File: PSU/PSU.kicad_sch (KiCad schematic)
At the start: 27 parts, among them J1 Screw_Terminal_01x02, U1 STPS10L25G-TR, U2 STPS10L25G-TR, U3 L4975A

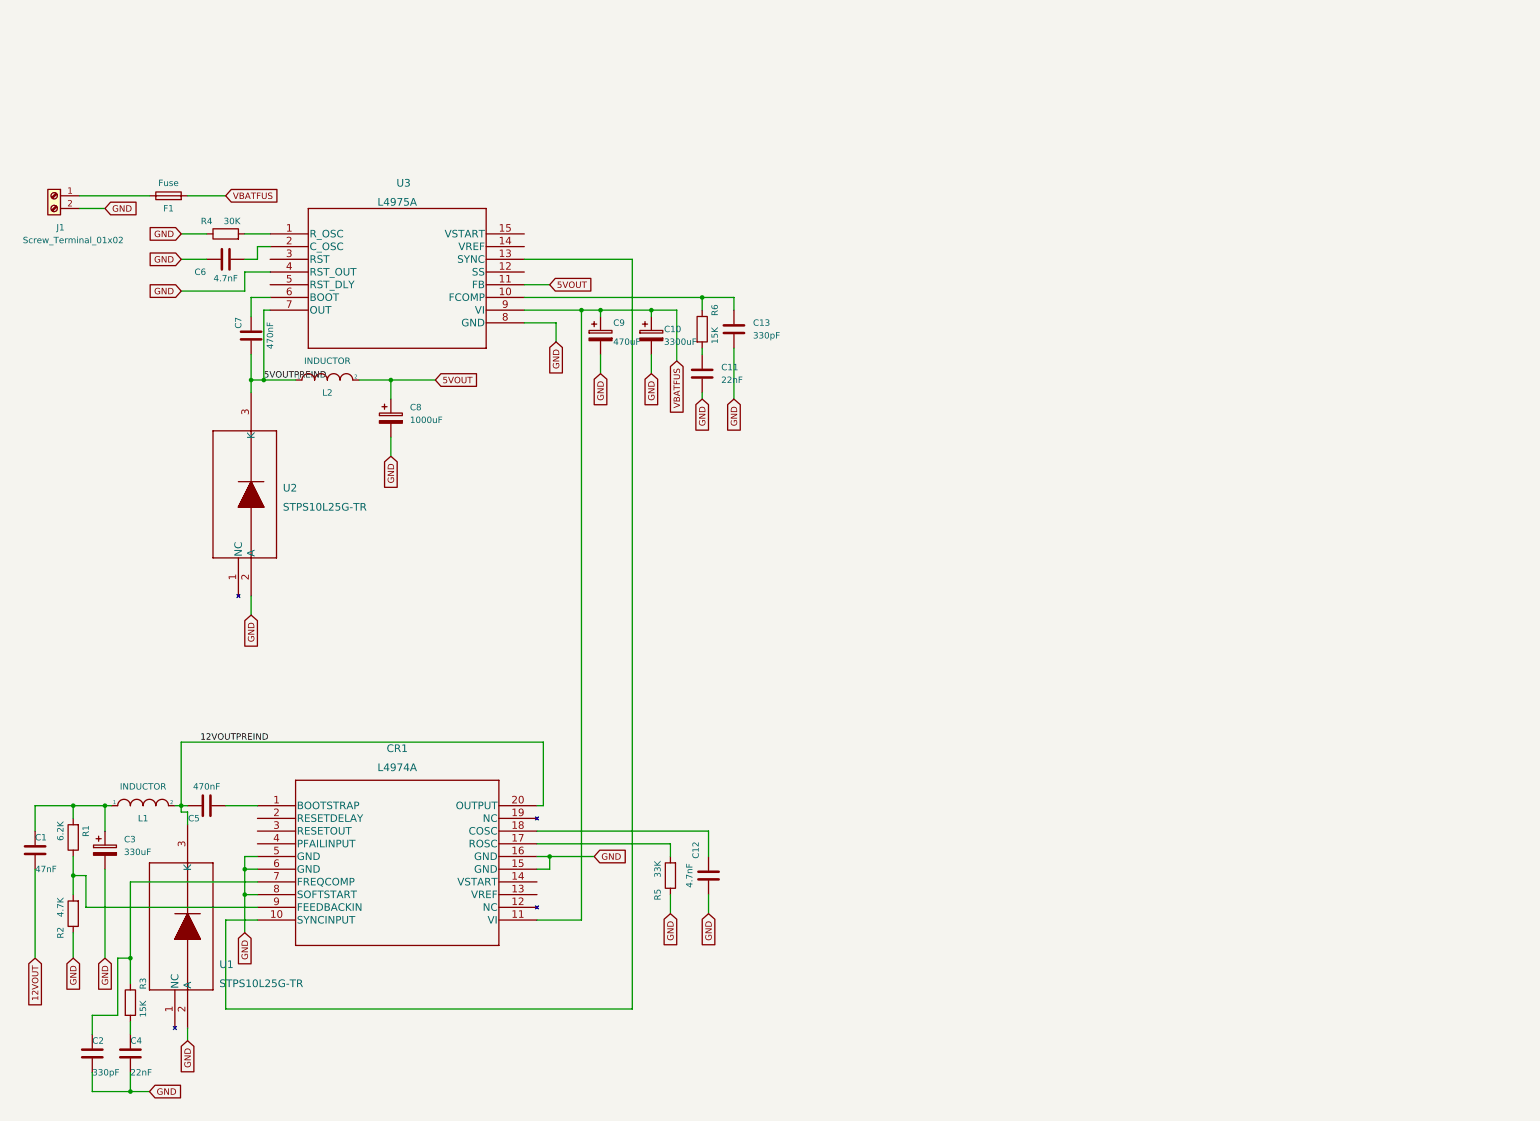
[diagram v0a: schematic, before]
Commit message: PCB placed and routed, more work to come
still need to check what's wrong with the schottky footprints
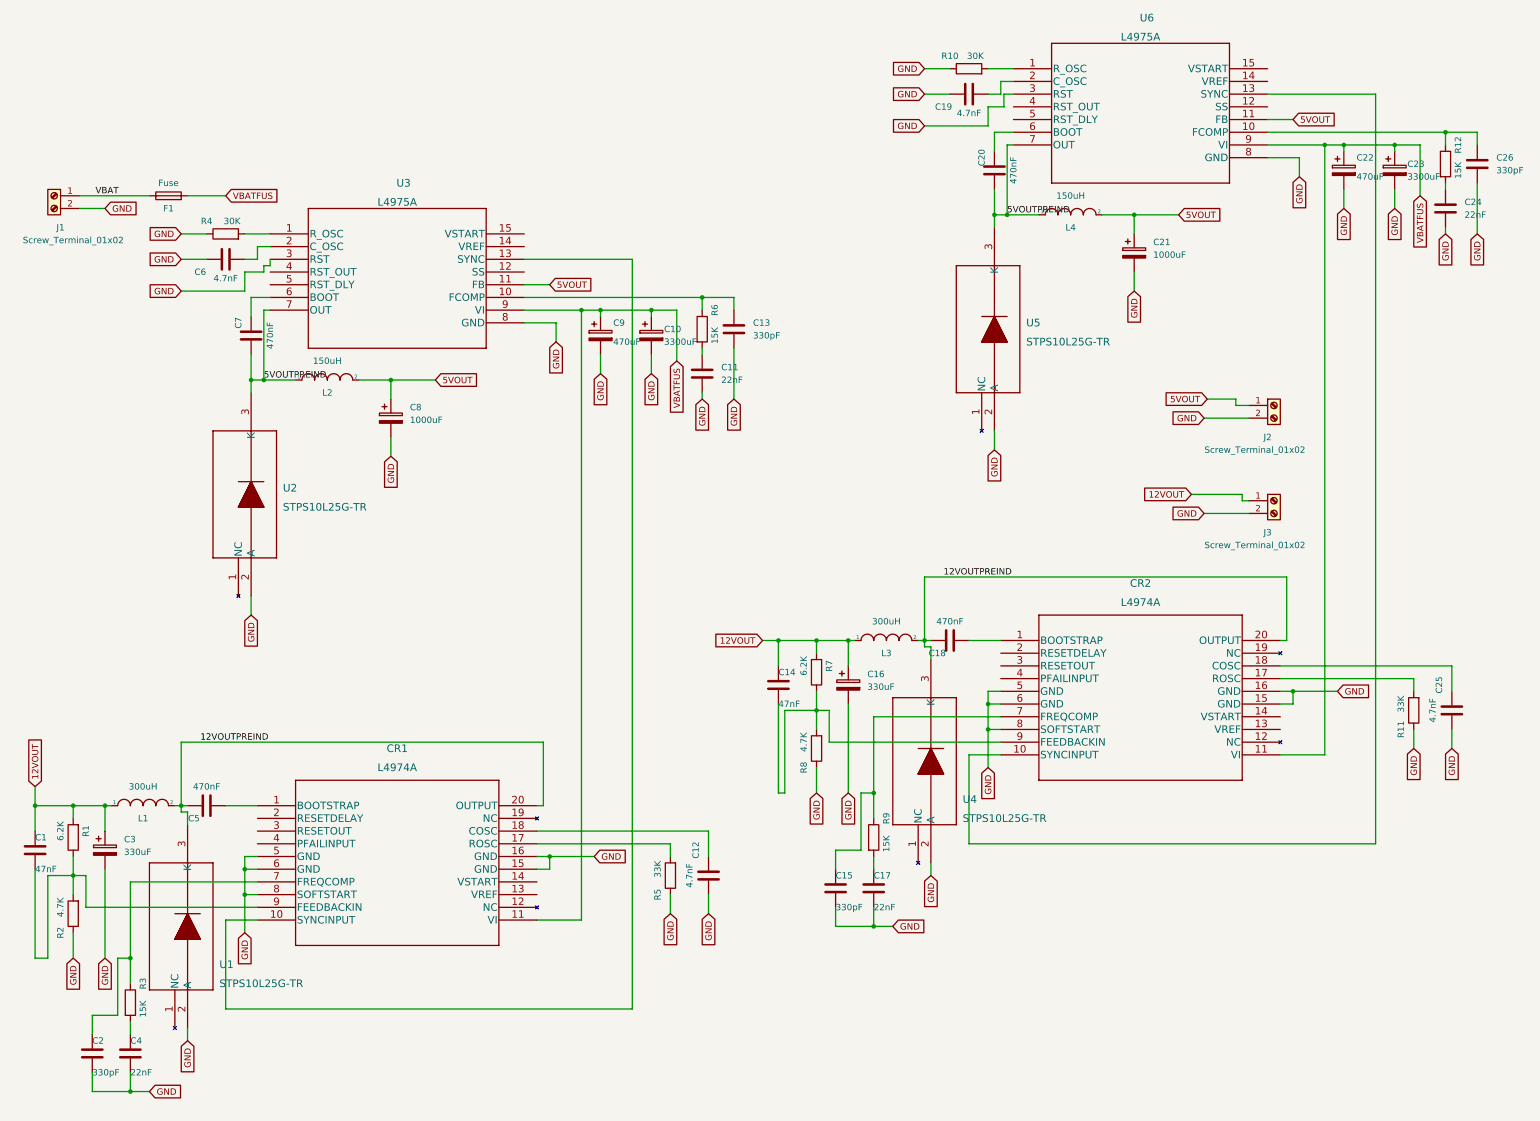
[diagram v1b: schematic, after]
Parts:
- added C14: 47nF, Capacitor_THT:C_Disc_D7.5mm_W5.0mm_P10.00mm, symbol Device:C
- added C15, C26: 330pF, Capacitor_THT:C_Disc_D7.5mm_W5.0mm_P10.00mm, symbol Device:C
- added C16: 330uF, Capacitor_THT:CP_Radial_D13.0mm_P5.00mm, symbol Device:C_Polarized
- added C17, C24: 22nF, Capacitor_THT:C_Disc_D7.5mm_W5.0mm_P10.00mm, symbol Device:C
- added C18, C20: 470nF, Capacitor_THT:C_Disc_D7.5mm_W5.0mm_P10.00mm, symbol Device:C
- added C19, C25: 4.7nF, Capacitor_THT:C_Disc_D7.5mm_W5.0mm_P10.00mm, symbol Device:C
- added C21: 1000uF, Capacitor_THT:CP_Radial_D13.0mm_P5.00mm, symbol Device:C_Polarized
- added C22: 470uF, Capacitor_THT:CP_Radial_D13.0mm_P5.00mm, symbol Device:C_Polarized
- added C23: 3300uF, Capacitor_THT:CP_Radial_D13.0mm_P5.00mm, symbol Device:C_Polarized
- added CR2: L4974A, L4974A:L4974A, symbol 2022-02-13_20-45-24:L4974A
- added J2, J3: Screw_Terminal_01x02, TerminalBlock:TerminalBlock_Altech_AK300-2_P5.00mm, symbol Connector:Screw_Terminal_01x02
- added L3: 300uH, Inductor_THT:L_Radial_D12.0mm_P10.00mm_Neosid_SD12_style1, symbol pspice:INDUCTOR
- added L4: 150uH, Inductor_THT:L_Radial_D12.0mm_P10.00mm_Neosid_SD12_style1, symbol pspice:INDUCTOR
- added R10: 30K, Resistor_THT:R_Axial_DIN0516_L15.5mm_D5.0mm_P20.32mm_Horizontal, symbol Device:R
- added R11: 33K, Resistor_THT:R_Axial_DIN0516_L15.5mm_D5.0mm_P20.32mm_Horizontal, symbol Device:R
- added R12, R9: 15K, Resistor_THT:R_Axial_DIN0516_L15.5mm_D5.0mm_P20.32mm_Horizontal, symbol Device:R
- added R7: 6.2K, Resistor_THT:R_Axial_DIN0516_L15.5mm_D5.0mm_P20.32mm_Horizontal, symbol Device:R
- added R8: 4.7K, Resistor_THT:R_Axial_DIN0516_L15.5mm_D5.0mm_P20.32mm_Horizontal, symbol Device:R
- added U4, U5: STPS10L25G-TR, STPS:STPS10L25G-TR, symbol 2022-02-13_20-55-28:STPS10L25G-TR
- added U6: L4975A, L4975A:L4975A, symbol 2022-02-13_20-41-58:L4975A
- L1: value INDUCTOR -> 300uH
- L2: value INDUCTOR -> 150uH
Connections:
- net 12VOUT: now also C1.1, C3.1, L1.1, R1.2, C14.1, C16.1, J3.1 (Pin_1), L3.1, R7.2; no longer C1.2
- net 12VOUTPREIND: now also C18.2, CR2.20 (OUTPUT), L3.2, U4.3 (K)
- net 5VOUT: now also C21.1, J2.1 (Pin_1), L4.2, U6.11 (FB)
- net 5VOUTPREIND: now also C20.1, L4.1, U5.3 (K), U6.7 (OUT)
- net GND: now also U3.3 (RST), C15.2, C16.2, C17.2, C19.1, C21.2, C22.2, C23.2, C24.2, C25.2, C26.2, CR2.15 (GND), CR2.16 (GND), CR2.5 (GND), CR2.6 (GND), CR2.8 (SOFTSTART), J2.2 (Pin_2), J3.2 (Pin_2), R10.1, R11.1, R8.1, U4.2 (A), U5.2 (A), U6.3 (RST), U6.8 (GND); no longer U3.4 (RST_OUT)
- net VBATFUS: now also C22.1, C23.1, CR2.11 (VI), U6.9 (VI)
- net at CR1.9 (FEEDBACKIN), R1.1, R2.2: now also C1.2
- net VBAT: now reaches F1.1, J1.1 (Pin_1)
- new net: C14.2, CR2.9 (FEEDBACKIN), R7.1, R8.2
- new net: R10.2, U6.1 (R_OSC)
- new net: C25.1, CR2.18 (COSC)
- new net: C26.1, R12.1, U6.10 (FCOMP)
- new net: CR2.10 (SYNCINPUT), U6.13 (SYNC)
- new net: C19.2, U6.2 (C_OSC)
- new net: C20.2, U6.6 (BOOT)
- new net: C24.1, R12.2
- new net: C15.1, CR2.7 (FREQCOMP), R9.1
- new net: CR2.17 (ROSC), R11.2
- new net: C17.1, R9.2
- new net: C18.1, CR2.1 (BOOTSTRAP)

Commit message: Revisited PCB
- SMT resistors instead of THT
- Added LEDs
- Added emergency stop button connector
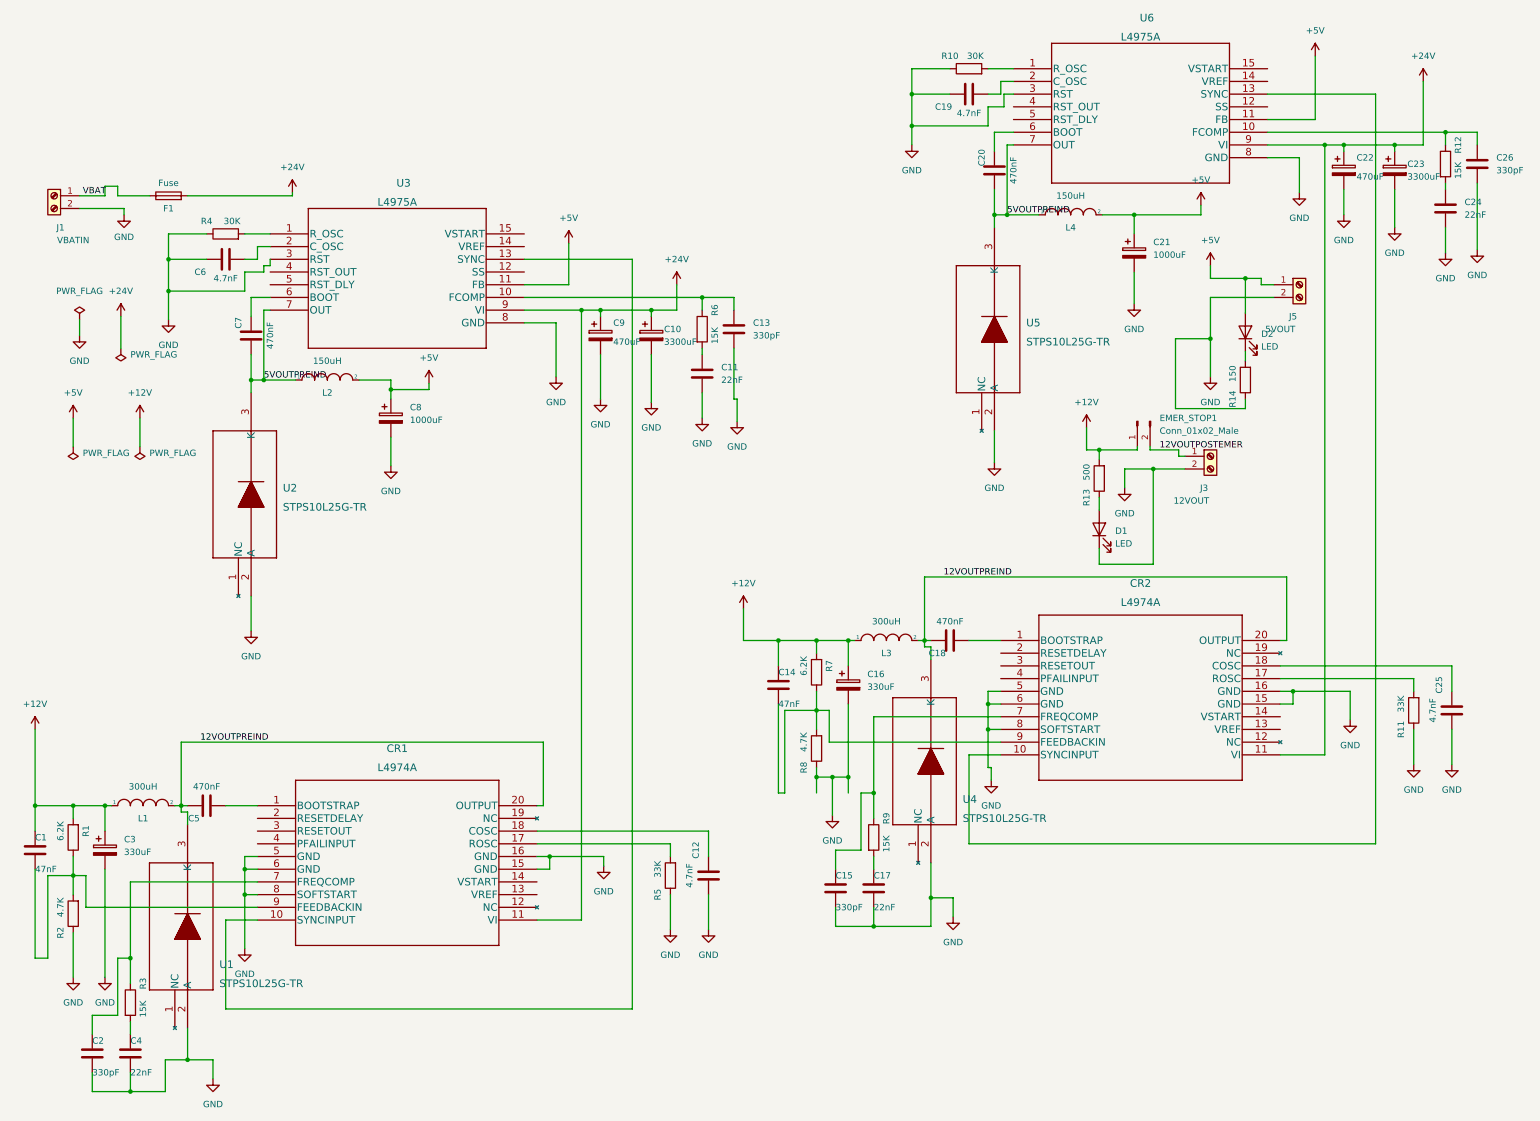
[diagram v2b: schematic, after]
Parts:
- added D1, D2: LED, LED_THT:LED_D5.0mm, symbol Device:LED
- added EMER_STOP1: Conn_01x02_Male, Connector_JST:JST_VH_B2P-VH-B_1x02_P3.96mm_Vertical, symbol Connector:Conn_01x02_Male
- added R13: 500, Resistor_SMD:R_0805_2012Metric, symbol Device:R
- added R14: 150, Resistor_SMD:R_0805_2012Metric, symbol Device:R
- C1, C11, C12, C13, C14, C15, C17, C18, C19, C2, C20, C24, C25, C26, C4, C5, C6, C7: footprint Capacitor_THT:C_Disc_D7.5mm_W5.0mm_P10.00mm -> Capacitor_SMD:C_0805_2012Metric
- J1: value Screw_Terminal_01x02 -> VBATIN
- J3: value Screw_Terminal_01x02 -> 12VOUT
- J5: renamed from J2; value Screw_Terminal_01x02 -> 5VOUT
- R1, R10, R11, R12, R2, R3, R4, R5, R6, R7, R8, R9: footprint Resistor_THT:R_Axial_DIN0516_L15.5mm_D5.0mm_P20.32mm_Horizontal -> Resistor_SMD:R_0805_2012Metric
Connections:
- net GND: now also D1.1 (K), R14.1
- net 12VOUT renamed +12V
- net +12V: now also EMER_STOP1.1 (Pin_1), R13.2; no longer J3.1 (Pin_1)
- net 5VOUT renamed +5V
- net +5V: now also D2.2 (A)
- net VBATFUS renamed +24V
- new net: D2.1 (K), R14.2
- new net: D1.2 (A), R13.1
- new net 12VOUTPOSTEMER: EMER_STOP1.2 (Pin_2), J3.1 (Pin_1)
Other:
- moved on the sheet: J3, J5

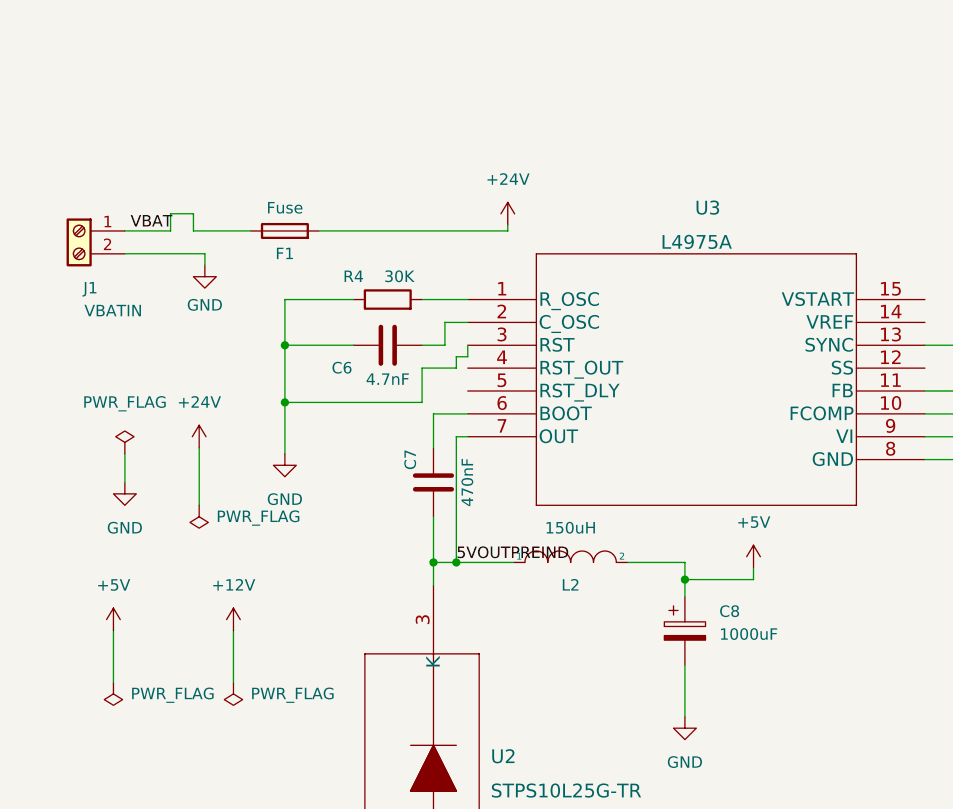
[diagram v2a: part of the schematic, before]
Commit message: Added switch and made space for inductors
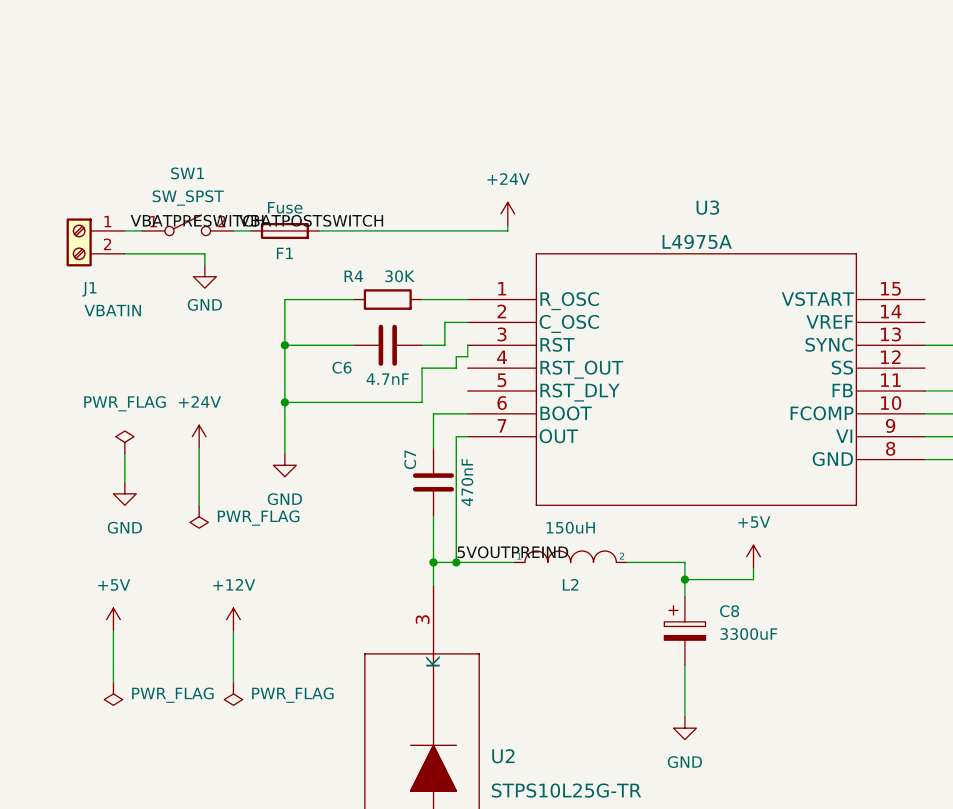
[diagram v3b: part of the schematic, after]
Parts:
- added SW1: SW_SPST, Connector_JST:JST_VH_B2P-VH_1x02_P3.96mm_Vertical, symbol Switch:SW_SPST
- C8: value 1000uF -> 3300uF
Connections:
- net VBAT renamed VBATPOSTSWITCH
- net VBATPOSTSWITCH: now also SW1.2 (B); no longer J1.1 (Pin_1)
- new net VBATPRESWITCH: J1.1 (Pin_1), SW1.1 (A)
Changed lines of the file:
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@@
-    (stroke (width 0) (type default) (color 0 0 0 0))
-  )
-  (wire (pts (xy 31.75 16.51) (xy 38.1 16.51))
     (stroke (width 0) (type default) (color 0 0 0 0))
   )
@@
     (stroke (width 0) (type default) (color 0 0 0 0))
   )
-  (wire (pts (xy 29.21 14.605) (xy 31.75 14.605))
-    (stroke (width 0) (type default) (color 0 0 0 0))
-  )
   (wire (pts (xy 26.67 191.77) (xy 26.67 195.58))
     (stroke (width 0) (type default) (color 0 0 0 0))
@@
     (stroke (width 0) (type default) (color 0 0 0 0))
   )
+  (wire (pts (xy 24.13 16.51) (xy 26.035 16.51))
+    (stroke (width 0) (type default) (color 0 0 0 0))
+  )
   (wire (pts (xy 118.11 148.59) (xy 128.905 148.59))
     (stroke (width 0) (type default) (color 0 0 0 0))
@@
     (stroke (width 0) (type default) (color 0 0 0 0))
   )
-  (wire (pts (xy 31.75 14.605) (xy 31.75 16.51))
-    (stroke (width 0) (type default) (color 0 0 0 0))
-  )
   (wire (pts (xy 57.15 148.59) (xy 59.69 148.59))
     (stroke (width 0) (type default) (color 0 0 0 0))
@@
     (stroke (width 0) (type default) (color 0 0 0 0))
   )
+  (wire (pts (xy 36.195 16.51) (xy 38.1 16.51))
+    (stroke (width 0) (type default) (color 0 0 0 0))
+  )
   (wire (pts (xy 267.97 8.89) (xy 261.62 8.89))
     (stroke (width 0) (type default) (color 0 0 0 0))
@@
     (stroke (width 0) (type default) (color 0 0 0 0))
   )
-  (wire (pts (xy 24.13 16.51) (xy 29.21 16.51))
-    (stroke (width 0) (type default) (color 0 0 0 0))
-  )
   (wire (pts (xy 271.145 -11.43) (xy 271.145 1.27))
     (stroke (width 0) (type default) (color 0 0 0 0))
@@
   )
   (wire (pts (xy 260.35 34.29) (xy 262.89 34.29))
-    (stroke (width 0) (type default) (color 0 0 0 0))
-  )
-  (wire (pts (xy 29.21 16.51) (xy 29.21 14.605))
     (stroke (width 0) (type default) (color 0 0 0 0))
   )
@@
     (effects (font (size 1.27 1.27)) (justify left bottom))
   )
-  (label "VBAT" (at 24.765 16.51 0)
+  (label "VBATPOSTSWITCH" (at 36.83 16.51 0)
     (effects (font (size 1.27 1.27)) (justify left bottom))
   )
@@
   )
   (label "12VOUTPREIND" (at 196.85 92.71 0)
+    (effects (font (size 1.27 1.27)) (justify left bottom))
+  )
+  (label "VBATPRESWITCH" (at 24.765 16.51 0)
     (effects (font (size 1.27 1.27)) (justify left bottom))
   )
@@
     (pin "1")
   )
+  (symbol (lib_id "Switch:SW_SPST") (at 31.115 16.51 0) (unit 1)
+    (in_bom yes) (on_board yes) (fields_autoplaced)
+    (property "Reference" "SW1" (id 0) (at 31.115 10.16 0))
+    (property "Value" "SW_SPST" (id 1) (at 31.115 12.7 0))
+    (property "Footprint" "Connector_JST:JST_VH_B2P-VH_1x02_P3.96mm_Vertical" (id 2) (at 31.115 16.51 0)
+      (effects (font (size 1.27 1.27)) hide)
+    )
+    (property "Datasheet" "~" (id 3) (at 31.115 16.51 0)
+      (effects (font (size 1.27 1.27)) hide)
+    )
+    (pin "1")
+    (pin "2")
+  )
   (symbol (lib_id "Device:C") (at 149.86 152.4 0) (unit 1)
     (in_bom yes) (on_board yes)
@@
       (effects (font (size 1.27 1.27)) (justify left))
     )
-    (property "Value" "1000uF" (id 1) (at 90.17 61.3409 0)
+    (property "Value" "3300uF" (id 1) (at 90.17 61.3409 0)
       (effects (font (size 1.27 1.27)) (justify left))
     )
@@
     )
     (path "/965c1acd-d75a-4a37-9ec4-13ca6e111c57"
-      (reference "C8") (unit 1) (value "1000uF") (footprint "Capacitor_THT:CP_Radial_D13.0mm_P5.00mm")
+      (reference "C8") (unit 1) (value "3300uF") (footprint "Capacitor_THT:CP_Radial_D13.0mm_P5.00mm")
     )
     (path "/3dbc85df-aaa7-4f46-8408-699725ad3be4"
@@
       (reference "R14") (unit 1) (value "150") (footprint "Resistor_SMD:R_0805_2012Metric")
     )
+    (path "/8c7cf97f-c542-425b-9742-26923471497b"
+      (reference "SW1") (unit 1) (value "SW_SPST") (footprint "Connector_JST:JST_VH_B2P-VH_1x02_P3.96mm_Vertical")
+    )
     (path "/c3405121-3fd8-420e-a2b2-ead5b99d24f7"
